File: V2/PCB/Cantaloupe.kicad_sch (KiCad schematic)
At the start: 121 parts, among them J1 USB_In, J2 OLED, J3 Link, J4 Debug, J5 Trackball, Q1 2N7002, Q2 AO3401A, SW1 MX, SW10 MX, SW11 MX, SW12 MX, SW13 MX, SW14 MX, SW15 MX, SW16 MX, SW17 MX, SW18 MX, SW19 MX, SW2 MX, SW20 MX, SW21 MX, SW22 MX, SW23 MX, SW24 MX, SW25 MX, SW26 MX, SW27 MX, SW28 MX, SW29 MX, SW3 MX, SW30 MX, SW31 Encoder, SW32 MX, SW4 MX, SW5 MX, SW6 MX, SW7 MX, SW8 MX, SW9 MX, U1 STM32F4x1CxUx, U2 SRV0504, U3 SRV0504, U4 XC6206P332MR, U5 LMV321, Y1 8MHz

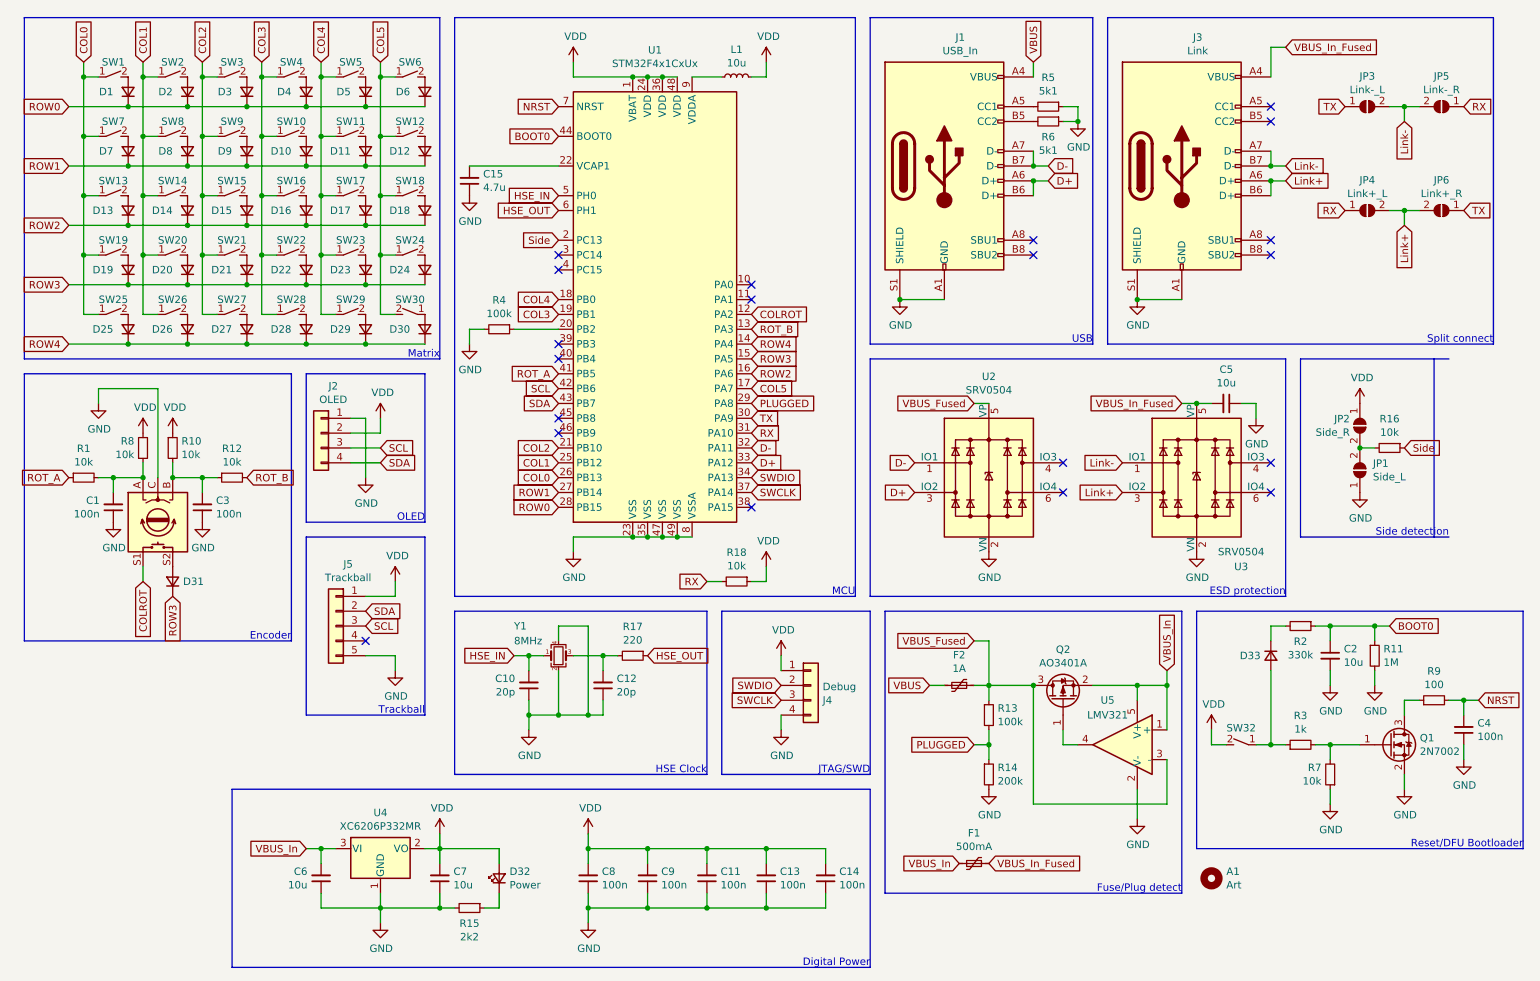
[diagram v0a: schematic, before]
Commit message: Update README.mdAdded silkscreen jumper guides. Connected indicator LED to spare GPIO. Updated images.
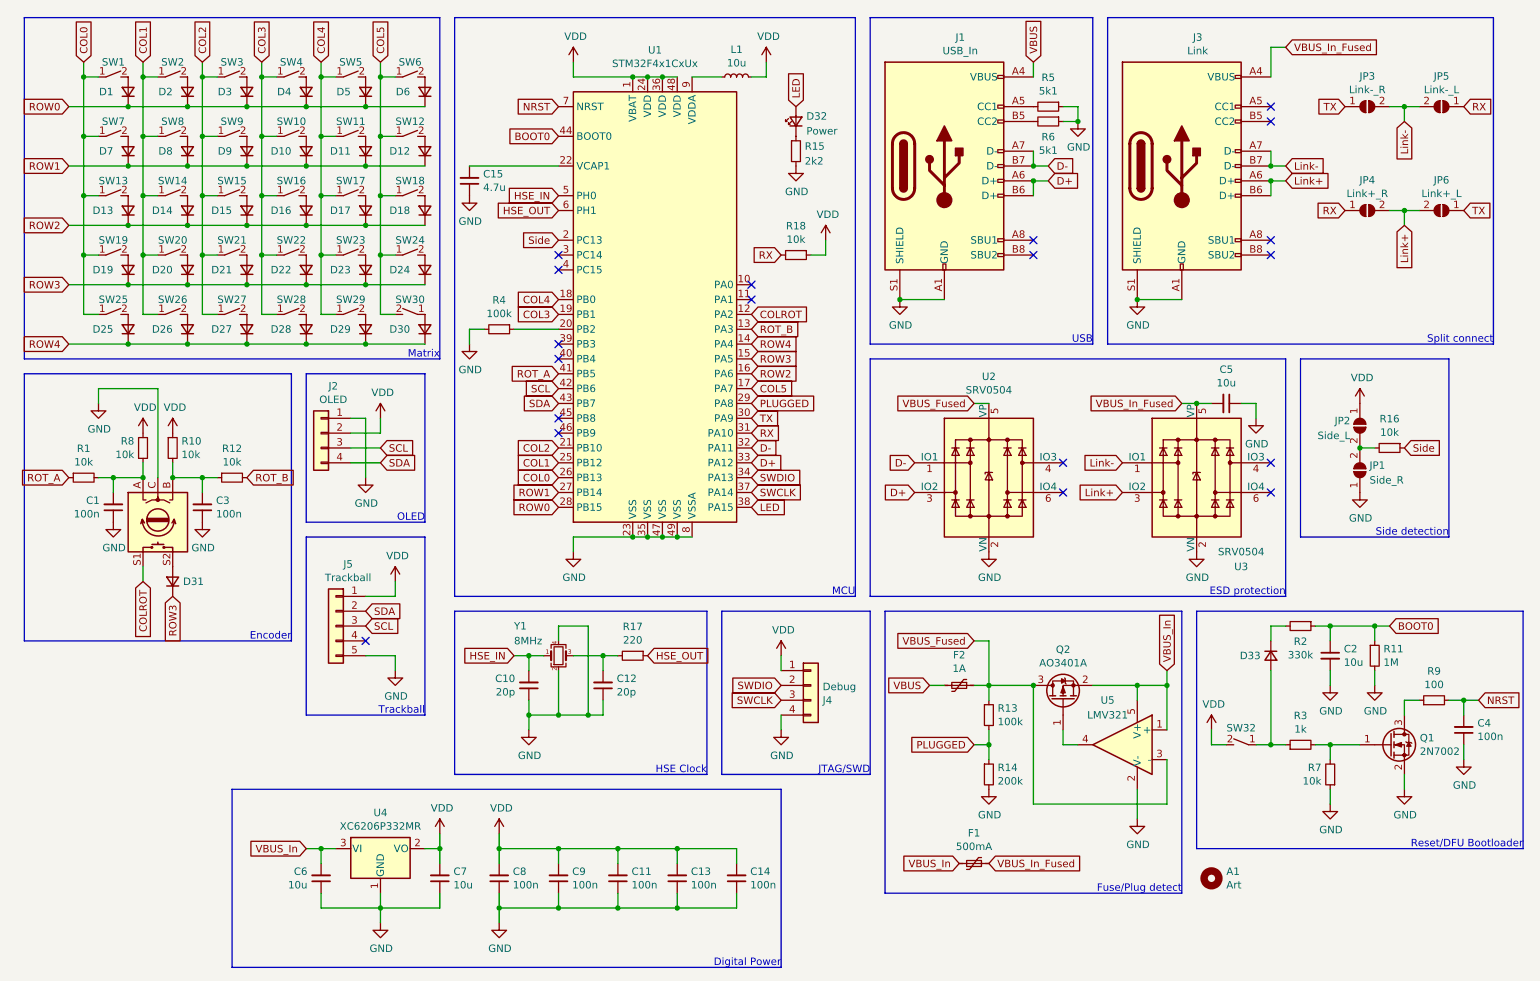
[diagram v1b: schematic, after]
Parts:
- JP1: value Side_L -> Side_R
- JP2: value Side_R -> Side_L
- JP3: value Link-_L -> Link-_R
- JP4: value Link+_L -> Link+_R
- JP5: value Link-_R -> Link-_L
- JP6: value Link+_R -> Link+_L
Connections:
- net VDD: no longer D32.2 (A)
- net LED: now reaches U1.38 (PA15)
- net LED: now also D32.2 (A)
- no-connect marks 20 -> 19
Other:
- moved on the sheet: C11, C13, C14, C8, C9, D32, R15, R18

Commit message: Update to PCB and case files, added cirque header, clean up of library
Added silkscreen jumper guides. Connected indicator LED to spare GPIO. Updated images. Added optional I2C resistors. New logo. New plate CAD files for potentiometer, trackball and trackpad options. Added header for Cirque trackpad. Cleaned up footprint library.
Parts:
- added J6: Trackpad, Ariamelon:FPC-SMD_FPC05012-09200-.5mm-rev, symbol Connector_Generic:Conn_01x12
- added R19, R20: 4.7k, Resistor_SMD:R_0603_1608Metric, symbol Device:R_Small
- A1: footprint Ariamelon:Catmelon -> Ariamelon:Ariamelon_Logo_x2
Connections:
- net GND: now also J6.11 (Pin_11)
- net SCL: now also J6.9 (Pin_9), R19.1
- net SDA: now also J6.10 (Pin_10), R20.1
- net VDD: now also J6.12 (Pin_12), R19.2, R20.2
- no-connect marks 19 -> 27
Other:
- note added: "Trackpad"
- moved on the sheet: J4

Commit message: Update to V2.1
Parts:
- removed J5: Trackball, Ariamelon:pimoroni_trackball_flippable, symbol Connector_Generic:Conn_01x05
- J5: renamed from J6; footprint Ariamelon:FPC-SMD_FPC05012-09200-.5mm-rev -> Connector_FFC-FPC:Hirose_FH12-12S-0.5SH_1x12-1MP_P0.50mm_Horizontal
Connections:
- net GND: now also J5.2 (Pin_2); no longer J5.11 (Pin_11)
- net SCL: now also J5.4 (Pin_4); no longer J5.9 (Pin_9)
- net SDA: now also J5.3 (Pin_3); no longer J5.10 (Pin_10)
- net VDD: now also J5.1 (Pin_1); no longer J5.12 (Pin_12)
- no-connect marks 27 -> 26
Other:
- note removed: "Trackball"
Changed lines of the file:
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@@
   (no_connect (at 30.48 160.02))
   (no_connect (at 109.22 58.42))
-  (no_connect (at 76.2 121.92))
   (no_connect (at 30.48 147.32))
   (no_connect (at 190.5 55.88))
@@
     (stroke (width 0) (type default) (color 0 0 0 0))
   )
-  (wire (pts (xy 81.28 114.3) (xy 81.28 111.76))
-    (stroke (width 0) (type default) (color 0 0 0 0))
-  )
   (polyline (pts (xy 200.66 15.24) (xy 200.66 71.12))
     (stroke (width 0) (type default) (color 0 0 0 0))
@@
     (stroke (width 0) (type default) (color 0 0 0 0))
   )
-  (polyline (pts (xy 86.36 104.14) (xy 66.04 104.14))
-    (stroke (width 0) (type default) (color 0 0 0 0))
-  )
   (wire (pts (xy 38.1 22.86) (xy 38.1 25.4))
     (stroke (width 0) (type default) (color 0 0 0 0))
@@
     (stroke (width 0) (type default) (color 0 0 0 0))
   )
-  (polyline (pts (xy 66.04 134.62) (xy 86.36 134.62))
-    (stroke (width 0) (type default) (color 0 0 0 0))
-  )
   (wire (pts (xy 129.54 165.1) (xy 129.54 167.64))
     (stroke (width 0) (type default) (color 0 0 0 0))
@@
     (stroke (width 0) (type default) (color 0 0 0 0))
   )
-  (wire (pts (xy 81.28 124.46) (xy 76.2 124.46))
-    (stroke (width 0) (type default) (color 0 0 0 0))
-  )
   (polyline (pts (xy 134.62 116.84) (xy 134.62 144.78))
     (stroke (width 0) (type default) (color 0 0 0 0))
@@
     (stroke (width 0) (type default) (color 0 0 0 0))
   )
-  (polyline (pts (xy 66.04 104.14) (xy 66.04 134.62))
-    (stroke (width 0) (type default) (color 0 0 0 0))
-  )
   (wire (pts (xy 60.96 35.56) (xy 58.42 35.56))
     (stroke (width 0) (type default) (color 0 0 0 0))
@@
     (stroke (width 0) (type default) (color 0 0 0 0))
   )
-  (polyline (pts (xy 86.36 134.62) (xy 86.36 104.14))
-    (stroke (width 0) (type default) (color 0 0 0 0))
-  )
   (wire (pts (xy 68.58 157.48) (xy 71.12 157.48))
     (stroke (width 0) (type default) (color 0 0 0 0))
@@
     (stroke (width 0) (type default) (color 0 0 0 0))
   )
-  (wire (pts (xy 81.28 127) (xy 81.28 124.46))
-    (stroke (width 0) (type default) (color 0 0 0 0))
-  )
   (wire (pts (xy 96.52 106.68) (xy 93.98 106.68))
     (stroke (width 0) (type default) (color 0 0 0 0))
@@
     (stroke (width 0) (type default) (color 0 0 0 0))
   )
-  (wire (pts (xy 76.2 114.3) (xy 81.28 114.3))
-    (stroke (width 0) (type default) (color 0 0 0 0))
-  )
   (wire (pts (xy 76.2 71.12) (xy 66.04 71.12))
     (stroke (width 0) (type default) (color 0 0 0 0))
@@
     (effects (font (size 1.27 1.27)) (justify right bottom))
   )
-  (text "Trackball" (at 86.36 134.62 180)
-    (effects (font (size 1.27 1.27)) (justify right bottom))
-  )
   (global_label "D-" (shape input) (at 170.18 91.44 180) (fields_autoplaced)
     (effects (font (size 1.27 1.27)) (justify right))
@@
     )
   )
-  (global_label "SCL" (shape input) (at 76.2 119.38 0) (fields_autoplaced)
-    (effects (font (size 1.27 1.27)) (justify left))
-    (property "Intersheet References" "${INTERSHEET_REFS}" (id 0) (at 0 0 0)
-      (effects (font (size 1.27 1.27)) hide)
-    )
-  )
   (global_label "ROW1" (shape input) (at 25.4 40.64 180) (fields_autoplaced)
     (effects (font (size 1.27 1.27)) (justify right))
@@
     )
   )
-  (global_label "SDA" (shape input) (at 76.2 116.84 0) (fields_autoplaced)
-    (effects (font (size 1.27 1.27)) (justify left))
-    (property "Intersheet References" "${INTERSHEET_REFS}" (id 0) (at 0 0 0)
-      (effects (font (size 1.27 1.27)) hide)
-    )
-  )
   (global_label "SDA" (shape input) (at 109.22 81.28 180) (fields_autoplaced)
     (effects (font (size 1.27 1.27)) (justify right))
@@
     (pin "1")
   )
-  (symbol (lib_id "Connector_Generic:Conn_01x05") (at 71.12 119.38 0) (mirror y) (unit 1)
-    (in_bom yes) (on_board yes)
-    (property "Reference" "J5" (id 0) (at 73.2028 108.7882 0))
-    (property "Value" "Trackball" (id 1) (at 73.2028 111.0996 0))
-    (property "Footprint" "Ariamelon:pimoroni_trackball_flippable" (id 2) (at 71.12 119.38 0)
-      (effects (font (size 1.27 1.27)) hide)
-    )
-    (property "Datasheet" "~" (id 3) (at 71.12 119.38 0)
-      (effects (font (size 1.27 1.27)) hide)
-    )
-    (pin "1")
-    (pin "2")
-    (pin "3")
-    (pin "4")
-    (pin "5")
-  )
-  (symbol (lib_id "power:VDD") (at 81.28 111.76 0) (unit 1)
-    (in_bom yes) (on_board yes)
-    (property "Reference" "#PWR0130" (id 0) (at 81.28 115.57 0)
-      (effects (font (size 1.27 1.27)) hide)
-    )
-    (property "Value" "VDD" (id 1) (at 81.661 107.3658 0))
-    (property "Footprint" "" (id 2) (at 81.28 111.76 0)
-      (effects (font (size 1.27 1.27)) hide)
-    )
-    (property "Datasheet" "" (id 3) (at 81.28 111.76 0)
-      (effects (font (size 1.27 1.27)) hide)
-    )
-    (pin "1")
-  )
   (symbol (lib_id "Device:R_Small") (at 182.88 144.78 0) (unit 1)
     (in_bom yes) (on_board yes)
@@
     (pin "1")
   )
-  (symbol (lib_id "power:GND") (at 81.28 127 0) (unit 1)
-    (in_bom yes) (on_board yes)
-    (property "Reference" "#PWR0131" (id 0) (at 81.28 133.35 0)
-      (effects (font (size 1.27 1.27)) hide)
-    )
-    (property "Value" "GND" (id 1) (at 81.407 131.3942 0))
-    (property "Footprint" "" (id 2) (at 81.28 127 0)
-      (effects (font (size 1.27 1.27)) hide)
-    )
-    (property "Datasheet" "" (id 3) (at 81.28 127 0)
-      (effects (font (size 1.27 1.27)) hide)
-    )
-    (pin "1")
-  )
   (symbol (lib_id "power:GND") (at 152.4 137.16 0) (mirror y) (unit 1)
     (in_bom yes) (on_board yes)
@@
     (pin "1")
   )
-  (symbol (lib_id "Connector_Generic:Conn_01x12") (at 35.56 149.86 0) (mirror x) (unit 1)
+  (symbol (lib_id "Connector_Generic:Conn_01x12") (at 35.56 147.32 0) (unit 1)
     (in_bom yes) (on_board yes) (fields_autoplaced)
-    (property "Reference" "J6" (id 0) (at 35.56 129.6502 0))
-    (property "Value" "Trackpad" (id 1) (at 35.56 132.1871 0))
-    (property "Footprint" "Ariamelon:FPC-SMD_FPC05012-09200-.5mm-rev" (id 2) (at 35.56 149.86 0)
+    (property "Reference" "J5" (id 0) (at 37.592 147.7553 0)
+      (effects (font (size 1.27 1.27)) (justify left))
+    )
+    (property "Value" "Trackpad" (id 1) (at 37.592 150.2922 0)
+      (effects (font (size 1.27 1.27)) (justify left))
+    )
+    (property "Footprint" "Connector_FFC-FPC:Hirose_FH12-12S-0.5SH_1x12-1MP_P0.50mm_Horizontal" (id 2) (at 35.56 147.32 0)
       (effects (font (size 1.27 1.27)) hide)
     )
-    (property "Datasheet" "~" (id 3) (at 35.56 149.86 0)
+    (property "Datasheet" "~" (id 3) (at 35.56 147.32 0)
       (effects (font (size 1.27 1.27)) hide)
     )
@@
       (reference "#PWR0129") (unit 1) (value "VDD") (footprint "")
     )
-    (path "/00000000-0000-0000-0000-0000624bb1ab"
-      (reference "#PWR0130") (unit 1) (value "VDD") (footprint "")
-    )
-    (path "/00000000-0000-0000-0000-0000625e0542"
-      (reference "#PWR0131") (unit 1) (value "GND") (footprint "")
-    )
     (path "/00000000-0000-0000-0000-0000624b93cd"
       (reference "#PWR0132") (unit 1) (value "VDD") (footprint "")
@@
       (reference "J4") (unit 1) (value "Debug") (footprint "Ariamelon:Debug_JTAG_SWD")
     )
-    (path "/00000000-0000-0000-0000-0000624ba1a7"
-      (reference "J5") (unit 1) (value "Trackball") (footprint "Ariamelon:pimoroni_trackball_flippable")
-    )
     (path "/5619f808-0333-40cf-b4ec-f3a4ff626417"
-      (reference "J6") (unit 1) (value "Trackpad") (footprint "Ariamelon:FPC-SMD_FPC05012-09200-.5mm-rev")
+      (reference "J5") (unit 1) (value "Trackpad") (footprint "Connector_FFC-FPC:Hirose_FH12-12S-0.5SH_1x12-1MP_P0.50mm_Horizontal")
     )
     (path "/00000000-0000-0000-0000-00006217adb6"
